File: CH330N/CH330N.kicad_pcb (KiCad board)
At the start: 2 copper layers, 15.5 x 20.3 mm, 20 parts, among them J2 Conn_01x06, P1 USB_C_Plug_USB2.0, U1 CH330N, U2 AP2127K-3.3

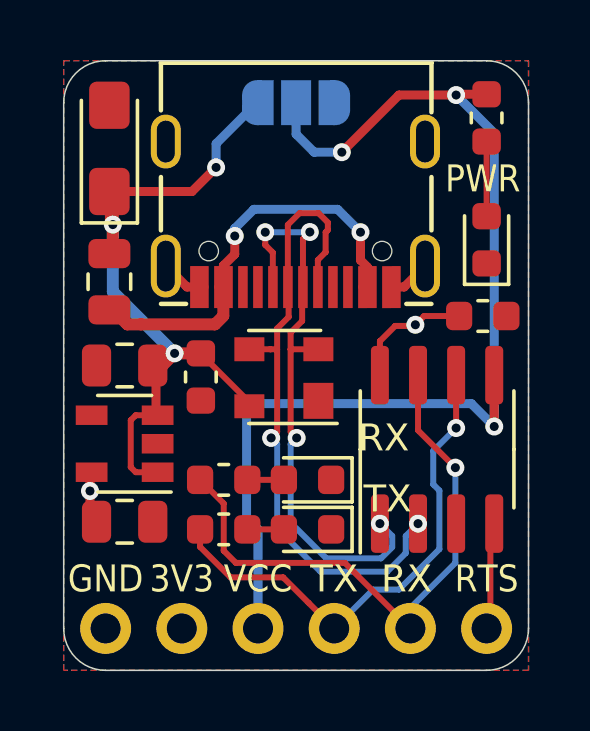
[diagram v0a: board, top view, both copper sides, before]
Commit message: Board Sizes Reduced in Width by 0.254mm
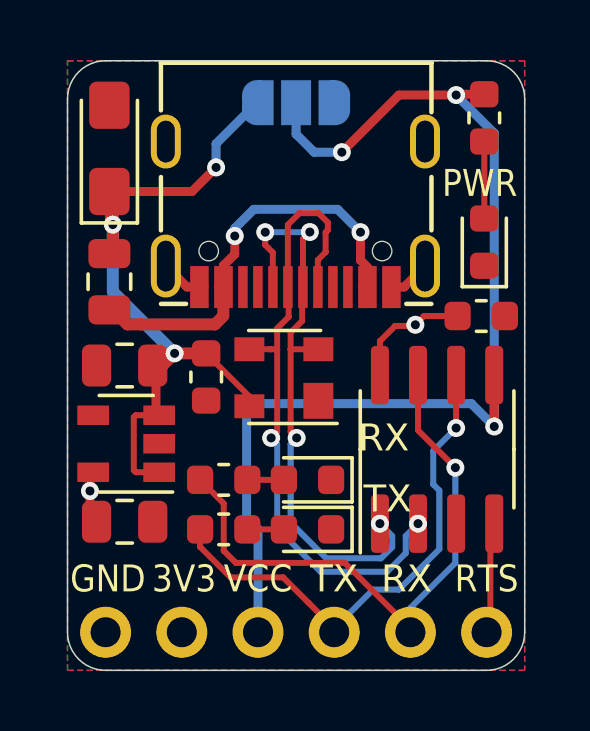
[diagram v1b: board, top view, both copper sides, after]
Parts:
- moved C4 0.18 mm to (64.2, 40.9)
- moved J2 0.13 mm to (73.5, 49.4)
- moved PWR 0.11 mm to (73.5, 36.4)
- moved R1 0.08 mm to (73.5, 32.3)
- moved C1 0.05 mm to (73.4, 38.9)
- moved U2 0.05 mm to (61.5, 43.1)
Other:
- board size 15.5 x 20.3 mm -> 15.2 x 20.3 mm

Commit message: Soldermask width adjusted
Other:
- rule solder_mask_min_width: 0.1 -> 0.05
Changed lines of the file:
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@@
     (pad_drill 1)
     (pad_to_mask_clearance 0)
-    (solder_mask_min_width 0.1)
+    (solder_mask_min_width 0.05)
     (aux_axis_origin 0 0)
     (visible_elements 7FFFFFFF)

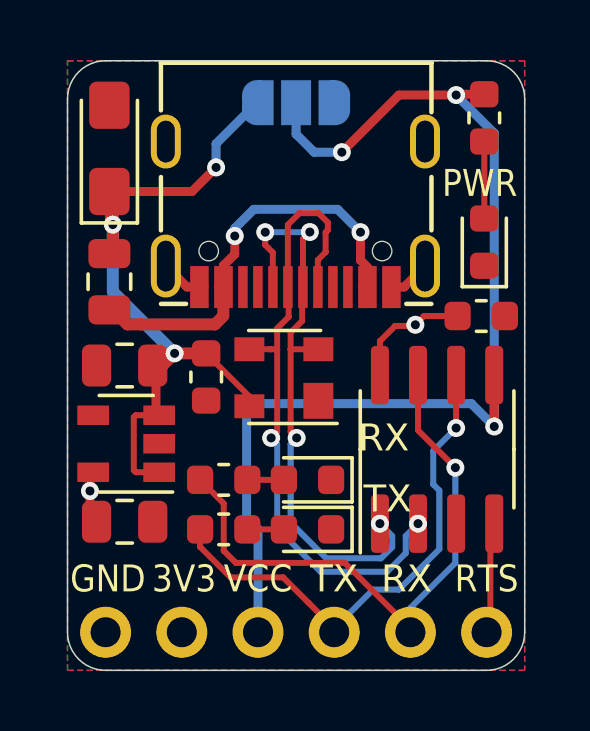
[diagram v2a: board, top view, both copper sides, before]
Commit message: SirUSB Updates
3D Renders changed to white solder mask. CH330N TX and RX references moved
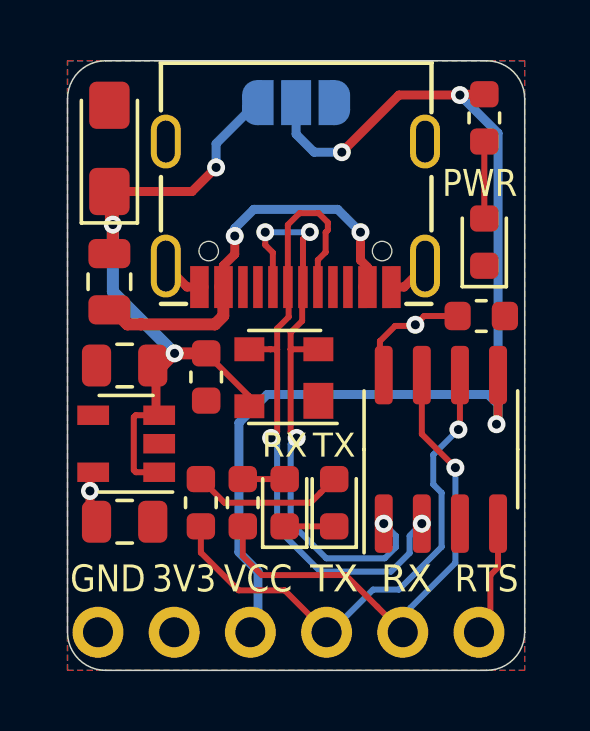
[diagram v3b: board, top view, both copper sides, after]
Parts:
- moved TX2 1.26 mm to (68.5, 45.1), turned to 90 degrees
- moved R2 1.17 mm to (64.0, 45.1), turned to 90 degrees
- moved RX1 1.08 mm to (66.8, 45.1), turned to 90 degrees
- moved R3 0.99 mm to (65.4, 45.1), turned to 90 degrees
- moved J2 0.25 mm to (73.3, 49.4)
- moved U1 0.13 mm to (72.0, 43.3)
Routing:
- net Net-(R2-Pad2): track 1.22 -> 5.10 mm
- net RX: track 19.6 -> 16.9 mm
- net GND: track 3.13 -> 4.78 mm

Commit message: SirUSB Updates
CH330N Revision 1.1 + 3D Render Improvement
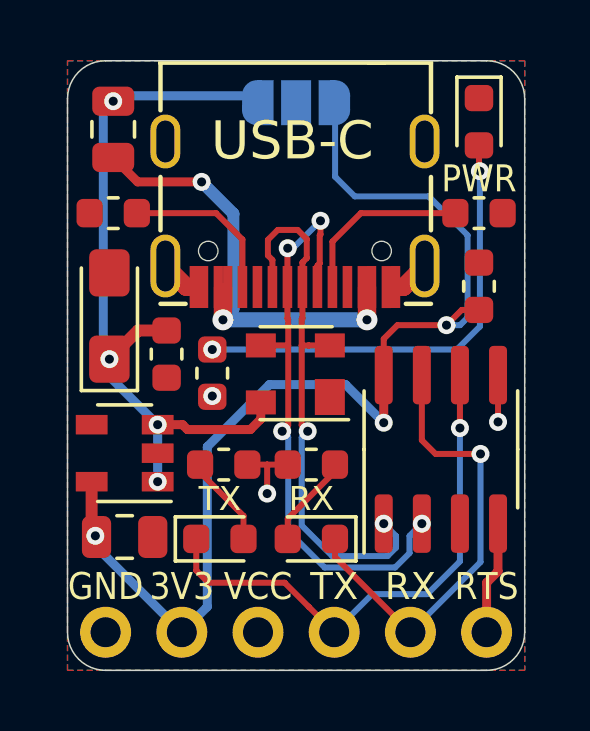
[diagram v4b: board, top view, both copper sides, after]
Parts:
- removed C6: 10uF, Capacitor_SMD:C_0805_2012Metric
- removed P1: USB_C_Plug_USB2.0, SirBoardLibrary:USB_C
- added R4: 5K1, Resistor_SMD:R_0603_1608Metric, F.Cu at (61.1, 35.4)
- added R5: 5K1, Resistor_SMD:R_0603_1608Metric, F.Cu at (73.3, 35.4)
- added USB-C: USB_C_Plug_USB2.0, SirBoardLibrary:USB_C, F.Cu at (70.4, 38.5)
- J2: footprint Connector_PinHeader_2.54mm:PinHeader_1x06_P2.54mm_Vertical -> Connector_PinHeader_2.54mm:PinHeader_1x06_P2.54mm_Horizontal; moved to F.Cu
- moved R1 12.4 mm to (64.4, 40.8), turned to 90 degrees
- moved C3 5.59 mm to (61.0, 38.9)
- moved F1 5.08 mm to (61.1, 32.6)
- moved PWR 4.02 mm to (73.3, 32.4), turned to 270 degrees
- moved TX2 4.00 mm to (64.6, 46.3), turned to 0 degrees
- moved R3 2.62 mm to (67.7, 43.8), turned to 0 degrees
- moved C4 1.52 mm to (62.9, 40.1)
- moved RX1 1.50 mm to (67.7, 46.3), turned to 180 degrees
- moved R2 1.48 mm to (64.8, 43.8), turned to 180 degrees
- moved C1 0.99 mm to (73.3, 37.9), turned to 270 degrees
- moved C7 0.51 mm to (61.5, 46.2)
- moved D1 0.40 mm to (67.2, 40.8)
- moved U2 0.32 mm to (61.5, 43.4)
- moved J2 0.25 mm to (73.5, 49.4), turned to 270 degrees
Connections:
- R2 pad 1: TX -> VCC
- R3 pad 1: RX -> VCC
- RX1 pad 1: GND -> RX
- TX2 pad 1: GND -> TX
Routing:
- net VCC: track 38.1 -> 3.87 mm
- net 3V3: track 5.67 -> 37.8 mm, vias 2 -> 3
- net Net-(PWR1-Pad2): track 2.49 -> 15.3 mm, vias 0 -> 2
- net Net-(P1-PadA5): track 0.00 -> 6.00 mm
- net Net-(P1-PadB5): track 0.00 -> 5.47 mm
- net Net-(F1-Pad2): track 15.4 -> 19.8 mm, vias 2 -> 3
- net Net-(R2-Pad2): track 5.10 -> 3.08 mm
- net Net-(R3-Pad2): track 1.40 -> 3.13 mm
- net D-: track 21.7 -> 20.0 mm, vias 2 -> 4
- net GND: track 4.78 -> 3.13 mm
- net RX: track 16.9 -> 15.4 mm
- net D+: track 19.5 -> 18.6 mm, vias 4 -> 2
- net TX: track 17.1 -> 17.9 mm
- net VBUS: track 24.7 -> 25.2 mm, vias 3 -> 4
- added copper zone on B.Cu, net VCC
- removed copper zone on B.Cu, net 3V3

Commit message: SirUSB Board Revisions
Removed MicroUSB Versions of FT230 and FT231, SolderPaste Layer Adjusted to -0.05mm, Silkscreens optimised, OSHW logo added.
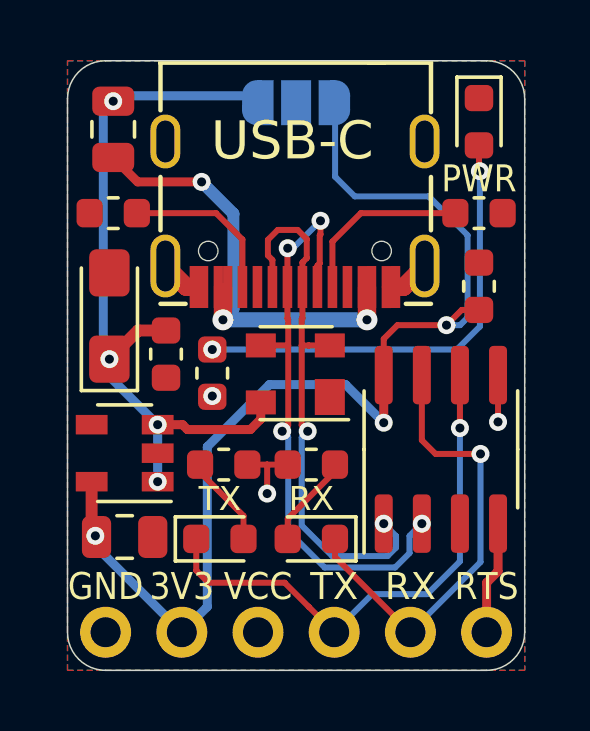
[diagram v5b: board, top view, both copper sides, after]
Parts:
- added G***: LOGO, logo:OSHW36x26, B.Cu at (73.3, 34.9)
- G***: footprint logo:logo76x107 -> logo:logo63x89
- G***: footprint logo:SirBoard98x31 -> logo:SirBoard112x35
- moved G*** 0.25 mm to (67.2, 43.4)
- moved G*** 0.13 mm to (67.2, 37.8)
